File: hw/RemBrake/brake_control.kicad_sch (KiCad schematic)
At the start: 45 parts, among them J7 Conn_01x07, J8 Conn_01x07, J9 Conn_01x03, Q6 BC337, Q7 BC847, Q8 BC337, Q9 BC847, U5 LM555xN, U6 BD5230G-TR

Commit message: fixed issue with the buzzer sound when charging is finished
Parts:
- added D4: MBR0520, Diode_SMD:D_SOD-123, symbol Device:D_Schottky
- renumbered C12 to C10, C8 to C11, C9 to C12, C10 to C7, C11 to C8, C7 to C9
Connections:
- net +5V: now also D4.2 (A); no longer M1.6 (V+)
- net VBUS: now also M1.6 (V+), D4.1 (K)
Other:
- moved on the sheet: C10, C7, C8

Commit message: added diodes to connect voltages to display and remote button even when connected to charger
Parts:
- removed D4: MBR0520, Diode_SMD:D_SOD-123, symbol Device:D_Schottky
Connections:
- net VBUS: no longer M1.6 (V+)
- new net VDD: M1.6 (V+)

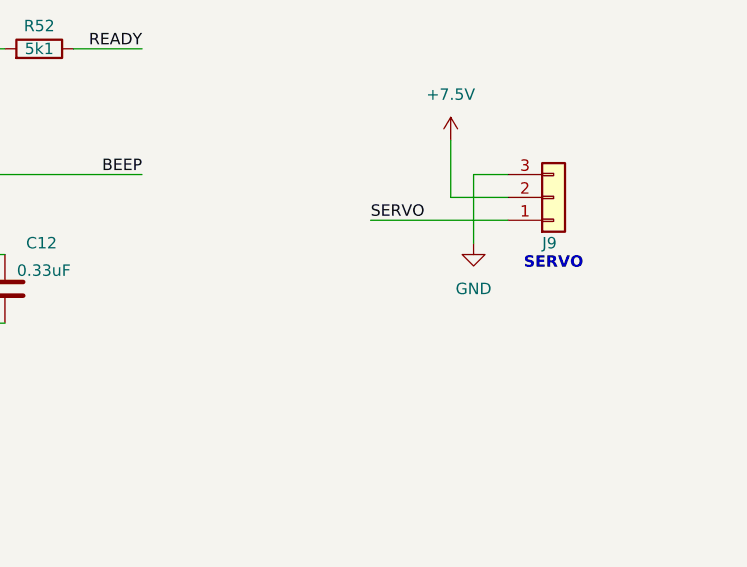
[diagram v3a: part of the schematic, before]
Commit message: added protection schottky diode on the servo
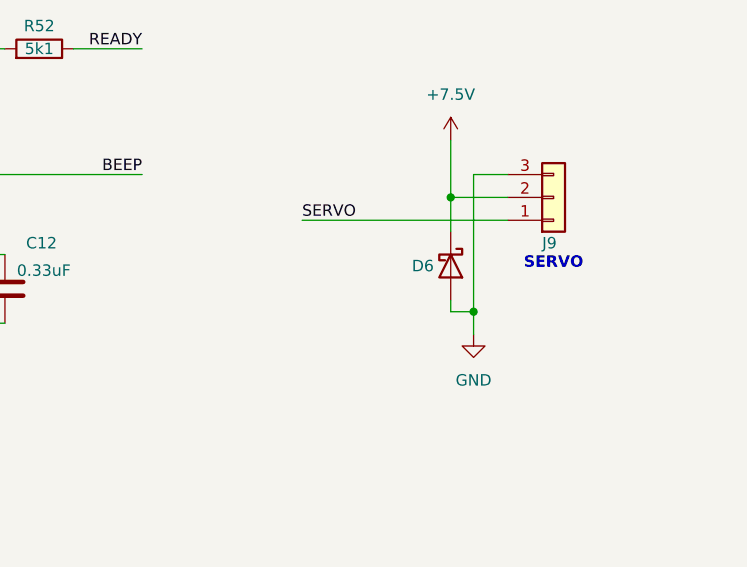
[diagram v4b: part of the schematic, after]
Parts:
- added D6: SS1200, Diode_SMD:D_SMA, symbol Diode:SS1200
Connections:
- net +7.5V: now also D6.1 (K)
- net GND: now also D6.2 (A)
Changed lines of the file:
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@@
 	)
 	(junction
+		(at 245.11 152.4)
+		(diameter 0)
+		(color 0 0 0 0)
+	)
+	(junction
 		(at 86.36 46.99)
 		(diameter 0)
@@
 	)
 	(junction
+		(at 242.57 139.7)
+		(diameter 0)
+		(color 0 0 0 0)
+	)
+	(junction
 		(at 66.04 115.57)
 		(diameter 0)
@@
 	(wire
 		(pts
+			(xy 245.11 154.94) (xy 245.11 152.4)
+		)
+		(stroke
+			(width 0)
+			(type default)
+		)
+	)
+	(wire
+		(pts
 			(xy 82.55 39.37) (xy 86.36 39.37)
 		)
@@
 	(wire
 		(pts
+			(xy 242.57 139.7) (xy 242.57 143.51)
+		)
+		(stroke
+			(width 0)
+			(type default)
+		)
+	)
+	(wire
+		(pts
 			(xy 124.46 27.94) (xy 138.43 27.94)
 		)
@@
 	(wire
 		(pts
+			(xy 242.57 152.4) (xy 245.11 152.4)
+		)
+		(stroke
+			(width 0)
+			(type default)
+		)
+	)
+	(wire
+		(pts
 			(xy 54.61 180.34) (xy 54.61 172.72)
 		)
@@
 	(wire
 		(pts
-			(xy 245.11 144.78) (xy 245.11 137.16)
+			(xy 245.11 152.4) (xy 245.11 137.16)
 		)
 		(stroke
@@
 	(wire
 		(pts
-			(xy 233.68 142.24) (xy 248.92 142.24)
+			(xy 226.06 142.24) (xy 248.92 142.24)
 		)
 		(stroke
@@
 	(wire
 		(pts
+			(xy 242.57 151.13) (xy 242.57 152.4)
+		)
+		(stroke
+			(width 0)
+			(type default)
+		)
+	)
+	(wire
+		(pts
 			(xy 142.24 76.2) (xy 142.24 90.17)
 		)
@@
 	)
 	(label "SERVO"
-		(at 233.68 142.24 0)
+		(at 226.06 142.24 0)
 		(effects
 			(font
@@
 	(symbol
 		(lib_id "power:GND")
-		(at 245.11 144.78 0)
+		(at 245.11 154.94 0)
 		(unit 1)
 		(exclude_from_sim no)
@@
 		(fields_autoplaced yes)
 		(property "Reference" "#PWR059"
-			(at 245.11 151.13 0)
+			(at 245.11 161.29 0)
 			(hide yes)
 			(effects
@@
 		)
 		(property "Value" "GND"
-			(at 245.11 149.86 0)
+			(at 245.11 160.02 0)
 			(effects
 				(font
@@
 		)
 		(property "Footprint" ""
-			(at 245.11 144.78 0)
+			(at 245.11 154.94 0)
 			(hide yes)
 			(effects
@@
 		)
 		(property "Datasheet" ""
-			(at 245.11 144.78 0)
+			(at 245.11 154.94 0)
 			(hide yes)
 			(effects
@@
 		)
 		(property "Description" "Power symbol creates a global label with name \"GND\" , ground"
-			(at 245.11 144.78 0)
+			(at 245.11 154.94 0)
 			(hide yes)
 			(effects
@@
 					(unit 1)
 				)
+			)
+		)
+	)
+	(symbol
+		(lib_id "Diode:SS1200")
+		(at 242.57 147.32 270)
+		(unit 1)
+		(exclude_from_sim no)
+		(in_bom yes)
+		(on_board yes)
+		(dnp no)
+		(property "Reference" "D6"
+			(at 238.252 147.32 90)
+			(effects
+				(font
+					(size 1.27 1.27)
+				)
+				(justify left)
+			)
+		)
+		(property "Value" "SS1200"
+			(at 245.11 148.2724 90)
+			(hide yes)
+			(effects
+				(font
+					(size 1.27 1.27)
+				)
+				(justify left)
+			)
+		)
+		(property "Footprint" "Diode_SMD:D_SMA"
+			(at 238.125 147.32 0)
+			(hide yes)
+			(effects
+				(font
+					(size 1.27 1.27)
+				)
+			)
+		)
+		(property "Datasheet" "https://www.wontop.com/uploadfiles/56/sort_excel/pdf/ss1150.pdf"
+			(at 242.57 147.32 0)
+			(hide yes)
+			(effects
+				(font
+					(size 1.27 1.27)
+				)
+			)
+		)
+		(property "Description" "200V 1A Schottky Diode, SMA"
+			(at 242.57 147.32 0)
+			(hide yes)
+			(effects
+				(font
+					(size 1.27 1.27)
+				)
+			)
+		)
+		(pin "2"
+		)
+		(pin "1"
+		)
+		(instances
+			(project ""
+				(path "/e6d4ae5b-c9d7-4cbe-b288-c929fdf55a75/4813b76c-f465-42f9-8515-5ce5d55b4403"
+					(reference "D6")
+					(unit 1)
+				)

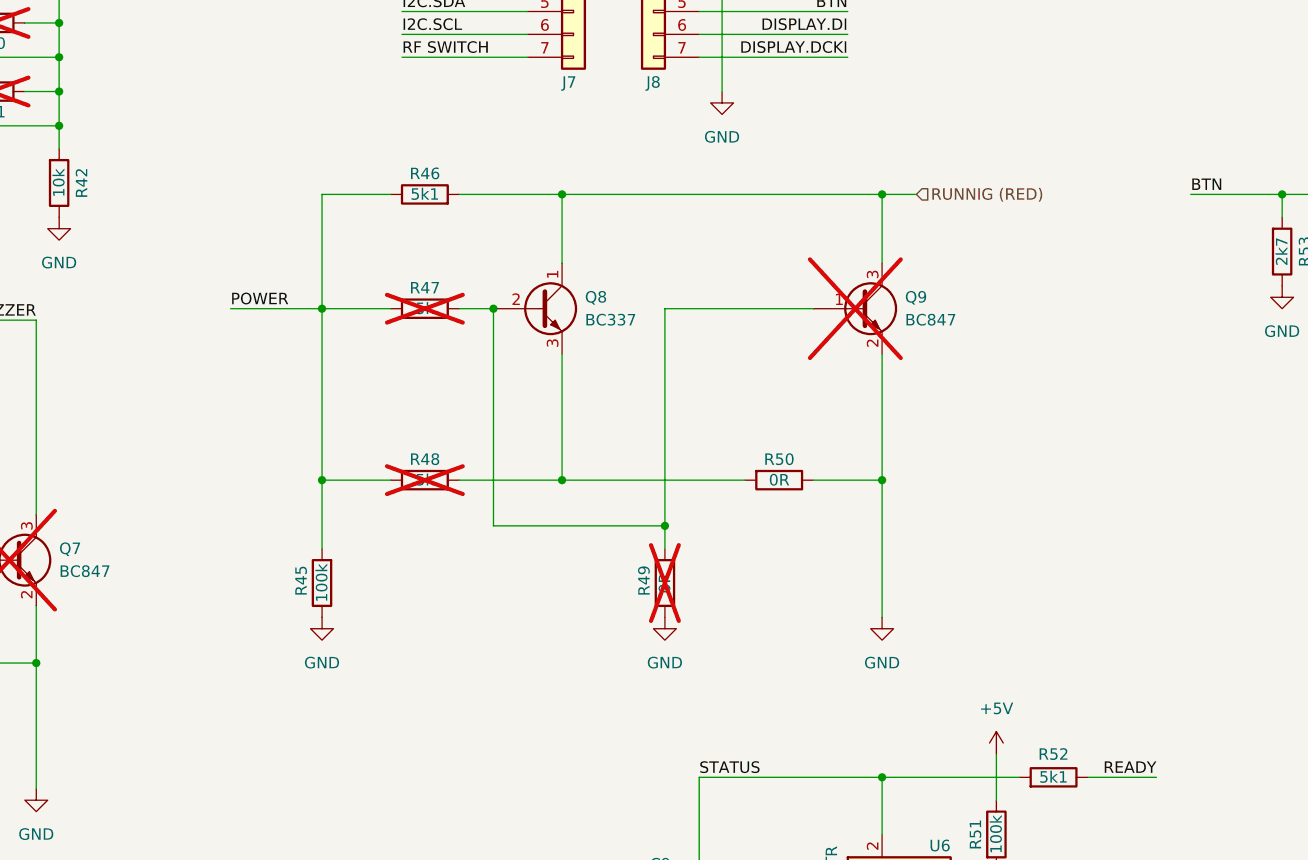
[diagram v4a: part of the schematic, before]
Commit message: adjusted connections to be able to use bc337
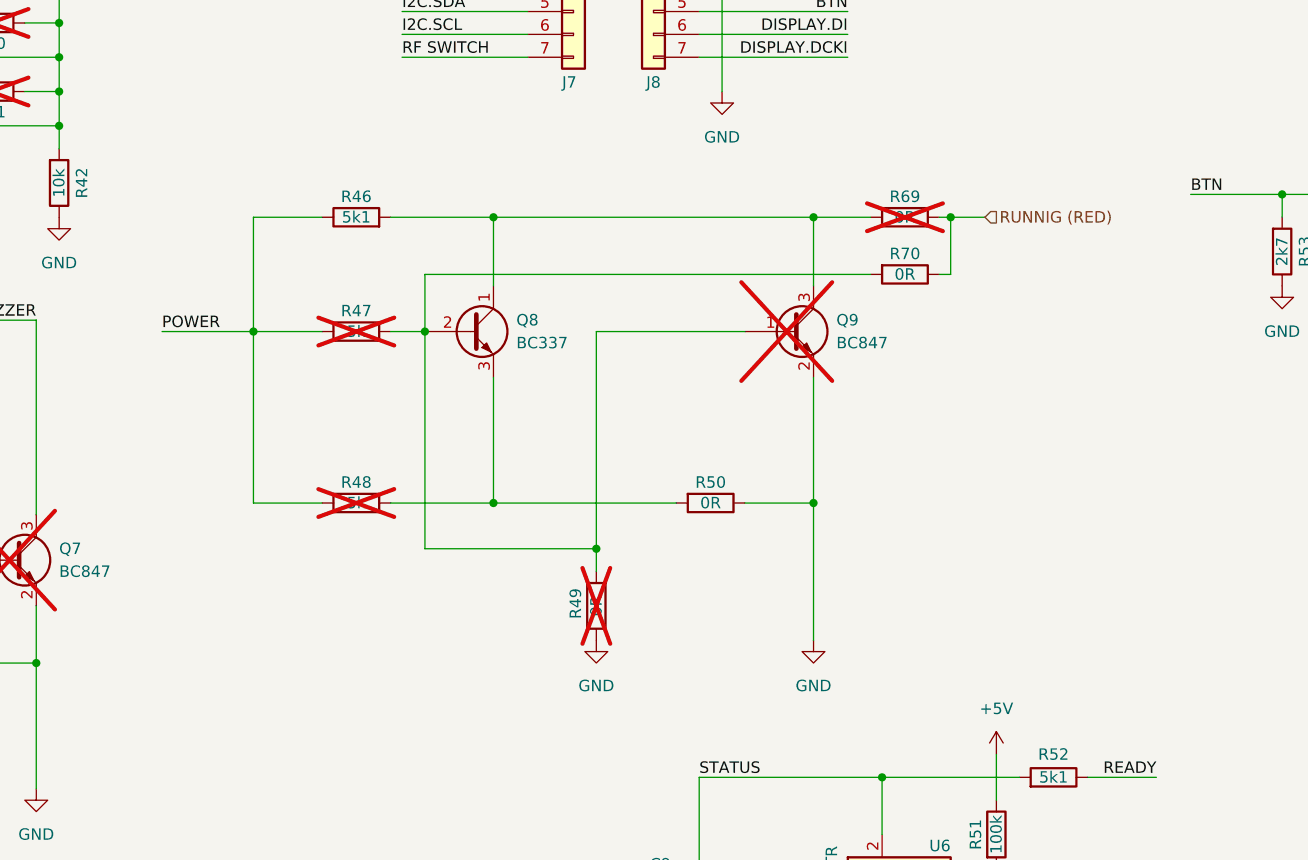
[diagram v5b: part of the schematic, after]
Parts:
- removed R45: 100k, Resistor_SMD:R_0805_2012Metric_Pad1.20x1.40mm_HandSolder, symbol Device:R
- added R69, R70: 0R, Resistor_SMD:R_0805_2012Metric_Pad1.20x1.40mm_HandSolder, symbol Device:R
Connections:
- net RUNNIG (RED): now also R69.1, R70.1; no longer Q8.1 (C), Q9.3 (C), R46.2
- net at Q8.2 (B), Q9.1 (B), R47.2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: now also R70.2
- new net: Q8.1 (C), Q9.3 (C), R46.2, R69.2
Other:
- moved on the sheet: Q8, Q9, R46, R47, R48, R49, R50

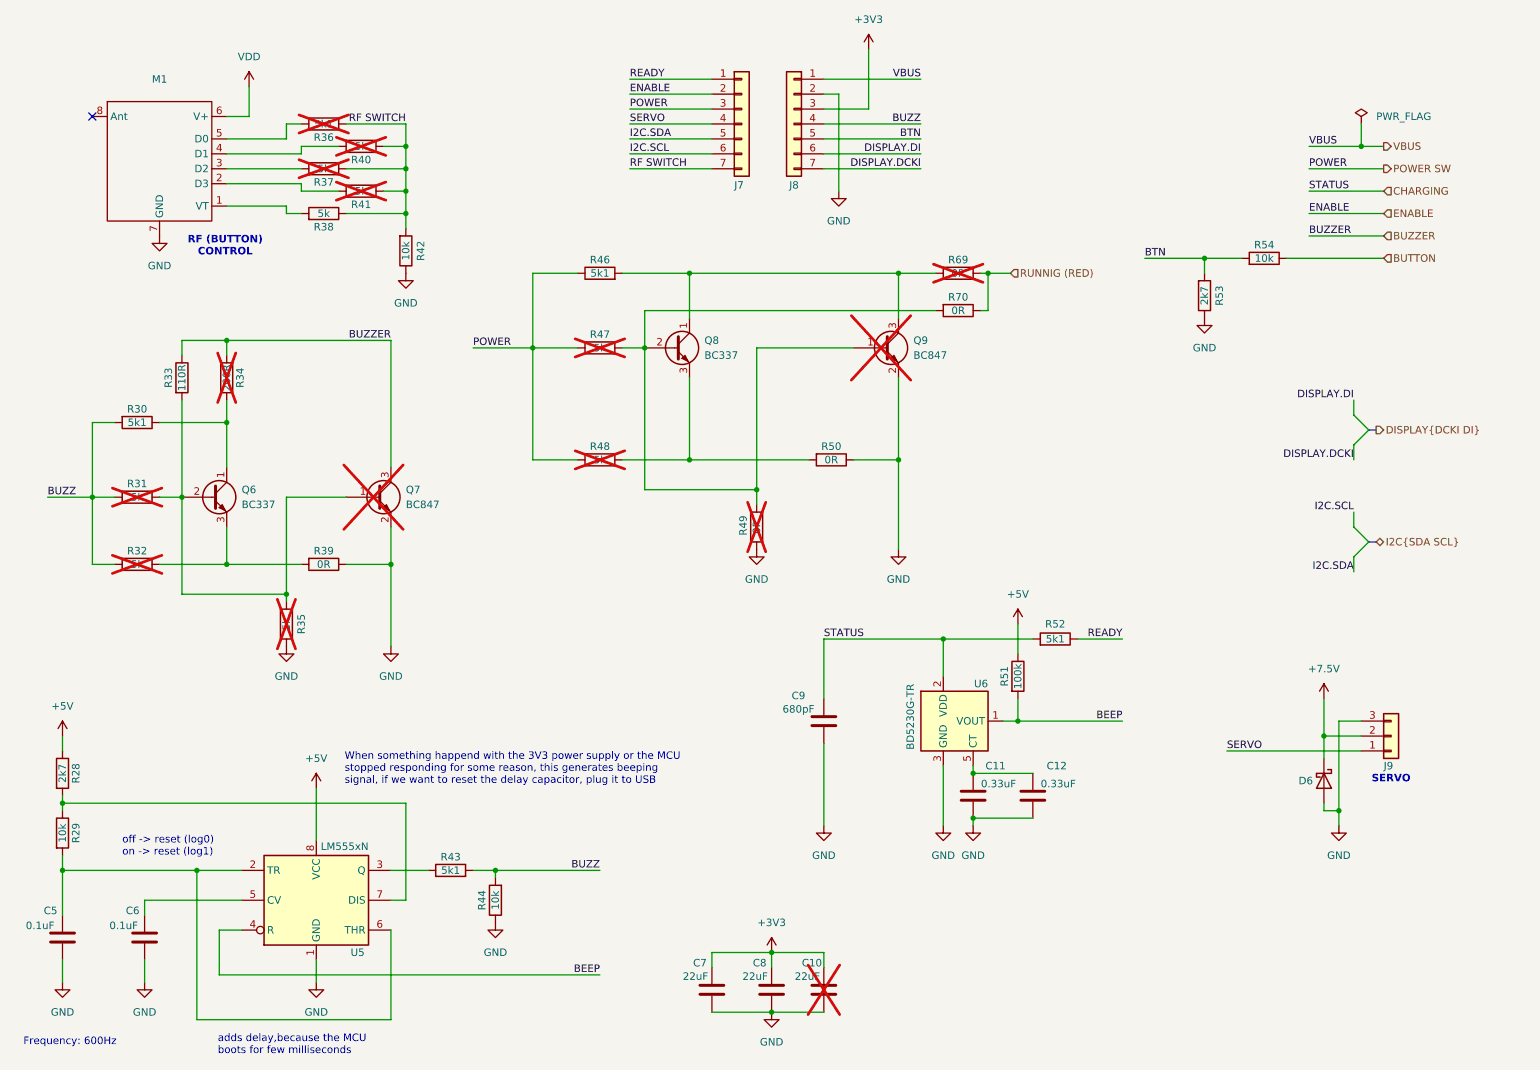
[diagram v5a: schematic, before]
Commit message: schematics update
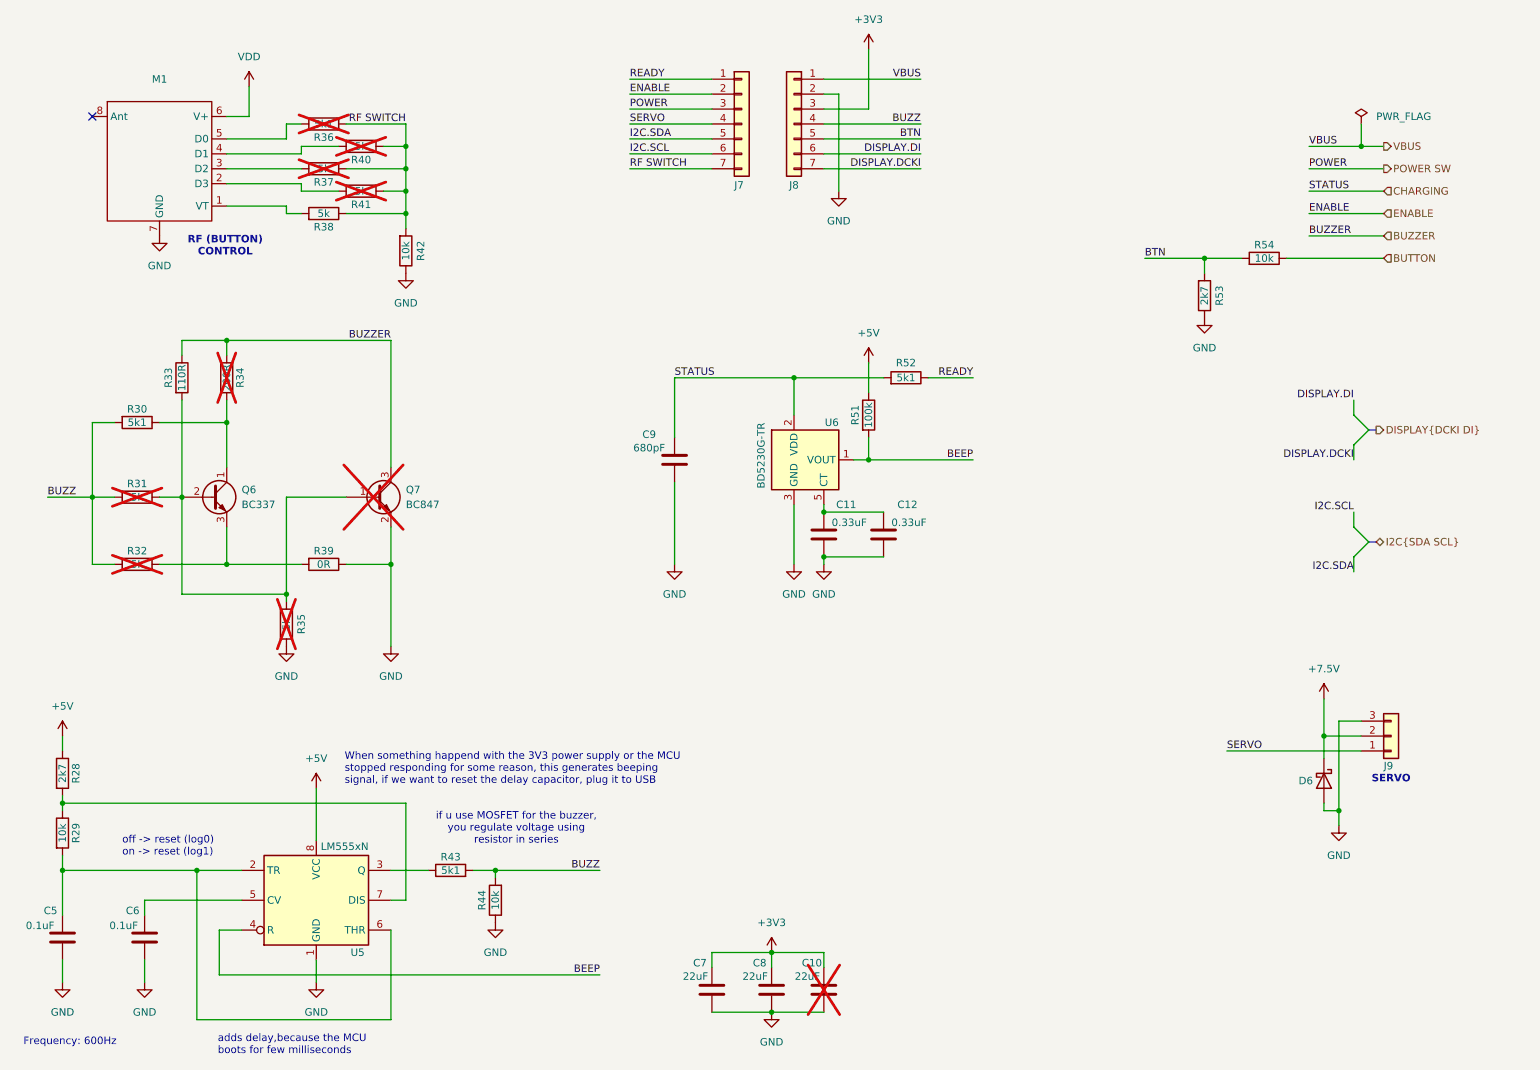
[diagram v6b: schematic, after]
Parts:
- removed Q8: BC337, Package_TO_SOT_THT:TO-92_Inline, symbol Transistor_BJT:BC337
- removed Q9: BC847, Package_TO_SOT_SMD:SOT-23, symbol Transistor_BJT:BC847
- removed R46: 5k1, Resistor_SMD:R_0805_2012Metric_Pad1.20x1.40mm_HandSolder, symbol Device:R
- removed R47, R48: 5k, Resistor_SMD:R_0805_2012Metric_Pad1.20x1.40mm_HandSolder, symbol Device:R
- removed R49, R50, R69, R70: 0R, Resistor_SMD:R_0805_2012Metric_Pad1.20x1.40mm_HandSolder, symbol Device:R
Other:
- note added: "if u use MOSFET for the buzzer, you regulate voltage using resistor in series"
- moved on the sheet: C11, C12, C9, R51, R52, U6
